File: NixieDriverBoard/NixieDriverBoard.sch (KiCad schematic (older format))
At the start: 9 parts, among them K155ID1 K155ID1, K155ID2 K155ID1

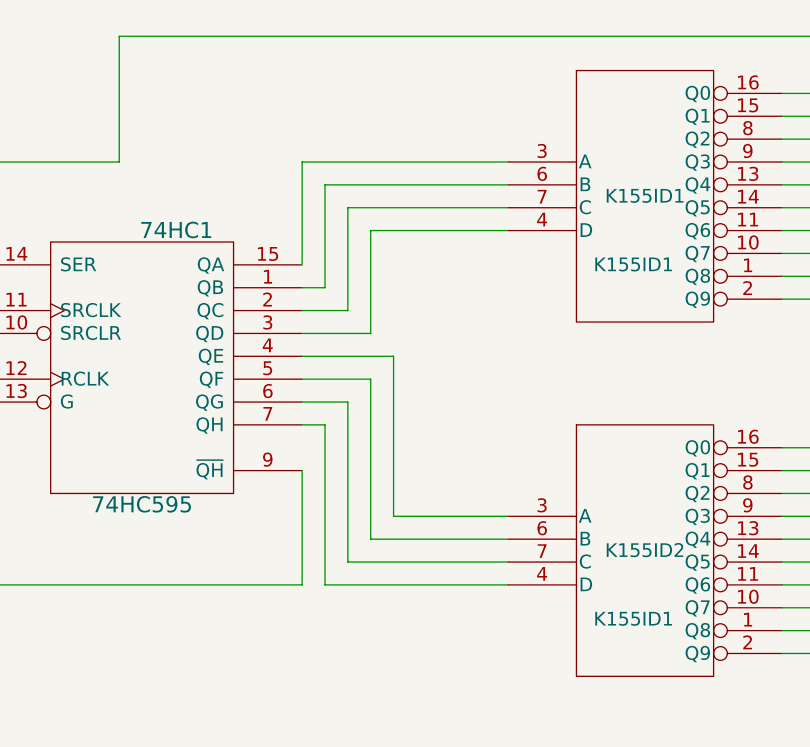
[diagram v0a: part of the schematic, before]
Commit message: Makes driver board more intuitive, and cleans up the silkscreen layers on both boards
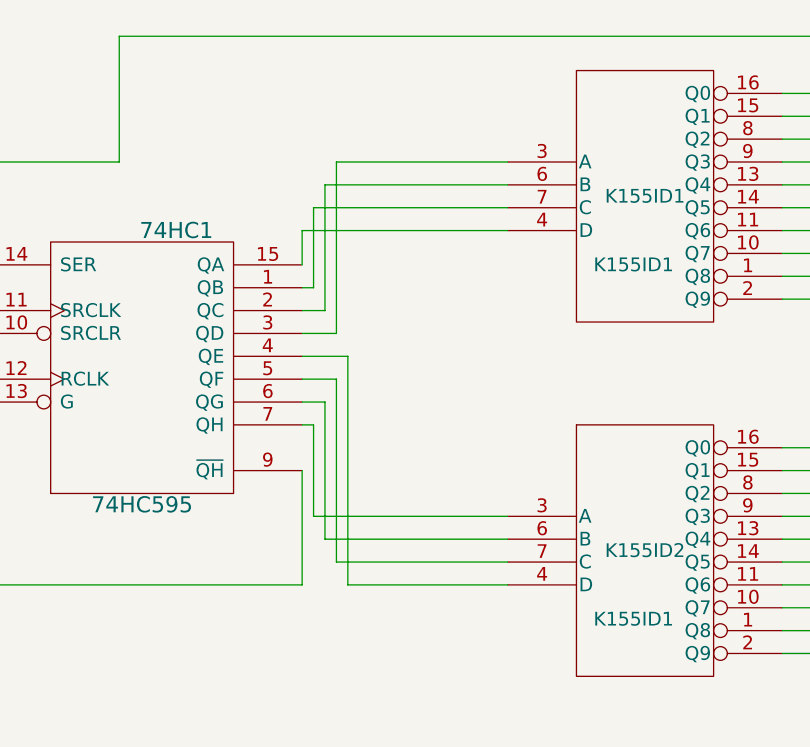
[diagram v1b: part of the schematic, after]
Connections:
- net at K155ID2.3 (A): now also 74HC1.7 (QH); no longer 74HC1.4 (QE)
- net at K155ID2.4 (D): now also 74HC1.4 (QE); no longer 74HC1.7 (QH)
- net at K155ID2.6 (B): now also 74HC1.6 (QG); no longer 74HC1.5 (QF)
- net at K155ID2.7 (C): now also 74HC1.5 (QF); no longer 74HC1.6 (QG)
- net at K155ID1.3 (A): now also 74HC1.3 (QD); no longer 74HC1.15 (QA)
- net at K155ID1.4 (D): now also 74HC1.15 (QA); no longer 74HC1.3 (QD)
- net at K155ID1.6 (B): now also 74HC1.2 (QC); no longer 74HC1.1 (QB)
- net at K155ID1.7 (C): now also 74HC1.1 (QB); no longer 74HC1.2 (QC)
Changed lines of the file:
@@
 LIBS:contrib
 LIBS:valves
-LIBS:NixieComponentLibrary
-LIBS:russian-nixies
 LIBS:NixieDriverBoard-cache
 EELAYER 25 0
@@
 $EndComp
 $Comp
-L 74HC595 74HC1
-U 1 1 5637B051
-P 5600 3650
-F 0 "74HC1" H 5750 4250 70  0000 C CNN
-F 1 "74HC595" H 5600 3050 70  0000 C CNN
-F 2 "Housings_DIP:DIP-16_W7.62mm_LongPads" H 5600 3650 60  0001 C CNN
-F 3 "" H 5600 3650 60  0000 C CNN
-	1    5600 3650
-	1    0    0    -1
-$EndComp
-$Comp
 L CONN_01X12 NIXIE1
 U 1 1 5637B08A
@@
 Connection ~ 3900 3400
 Wire Wire Line
-	6300 3200 6300 2750
-Wire Wire Line
-	6300 2750 7200 2750
-Wire Wire Line
-	6300 3300 6400 3300
-Wire Wire Line
-	6400 3300 6400 2850
-Wire Wire Line
-	6400 2850 7200 2850
-Wire Wire Line
-	6300 3400 6500 3400
-Wire Wire Line
-	6500 3400 6500 2950
-Wire Wire Line
-	6500 2950 7200 2950
-Wire Wire Line
-	6300 3500 6600 3500
-Wire Wire Line
-	6600 3500 6600 3050
-Wire Wire Line
-	6600 3050 7200 3050
-Wire Wire Line
-	6300 3900 6400 3900
-Wire Wire Line
-	6400 3900 6400 4600
-Wire Wire Line
-	6400 4600 7200 4600
-Wire Wire Line
-	6300 3800 6500 3800
-Wire Wire Line
-	6500 3800 6500 4500
-Wire Wire Line
-	6500 4500 7200 4500
-Wire Wire Line
-	6300 3700 6600 3700
-Wire Wire Line
-	6600 3700 6600 4400
-Wire Wire Line
-	6600 4400 7200 4400
-Wire Wire Line
-	6300 3600 6700 3600
-Wire Wire Line
-	6700 3600 6700 4300
-Wire Wire Line
-	6700 4300 7200 4300
-Wire Wire Line
 	5500 2750 5500 2200
 Connection ~ 3600 2750
@@
 Wire Wire Line
 	9050 3900 9300 3900
+$Comp
+L 74HC595 74HC1
+U 1 1 5637B051
+P 5600 3650
+F 0 "74HC1" H 5750 4250 70  0000 C CNN
+F 1 "74HC595" H 5600 3050 70  0000 C CNN
+F 2 "Housings_DIP:DIP-16_W7.62mm_LongPads" H 5600 3650 60  0001 C CNN
+F 3 "" H 5600 3650 60  0000 C CNN
+	1    5600 3650
+	1    0    0    -1
+$EndComp
+Wire Wire Line
+	6300 3200 6300 3050
+Wire Wire Line
+	6300 3050 7200 3050
+Wire Wire Line
+	6300 3300 6350 3300
+Wire Wire Line
+	6350 3300 6350 2950
+Wire Wire Line
+	6350 2950 7200 2950
+Wire Wire Line
+	6300 3400 6400 3400
+Wire Wire Line
+	6400 3400 6400 2850
+Wire Wire Line
+	6400 2850 7200 2850
+Wire Wire Line
+	6300 3500 6450 3500
+Wire Wire Line
+	6450 3500 6450 2750
+Wire Wire Line
+	6450 2750 7200 2750
+Wire Wire Line
+	6300 3900 6350 3900
+Wire Wire Line
+	6350 3900 6350 4300
+Wire Wire Line
+	6350 4300 7200 4300
+Wire Wire Line
+	6300 3800 6400 3800
+Wire Wire Line
+	6400 3800 6400 4400
+Wire Wire Line
+	6400 4400 7200 4400
+Wire Wire Line
+	6300 3700 6450 3700
+Wire Wire Line
+	6450 3700 6450 4500
+Wire Wire Line
+	6450 4500 7200 4500
+Wire Wire Line
+	6300 3600 6500 3600
+Wire Wire Line
+	6500 3600 6500 4600
+Wire Wire Line
+	6500 4600 7200 4600
 $EndSCHEMATC
